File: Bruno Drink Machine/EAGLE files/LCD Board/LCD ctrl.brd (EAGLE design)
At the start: 82.5 x 76.2 mm, 36 parts, among them IC1 PIC24FJ256DA210-I/PT, IC2 IS62LV256AL, IC3 IS62LV256AL, IC4 BA3259H-HRP5, P1 CONN-40P-62684-401100ALF, P18 CONN-8P-PND, P2 USB-CON690-005-299-043

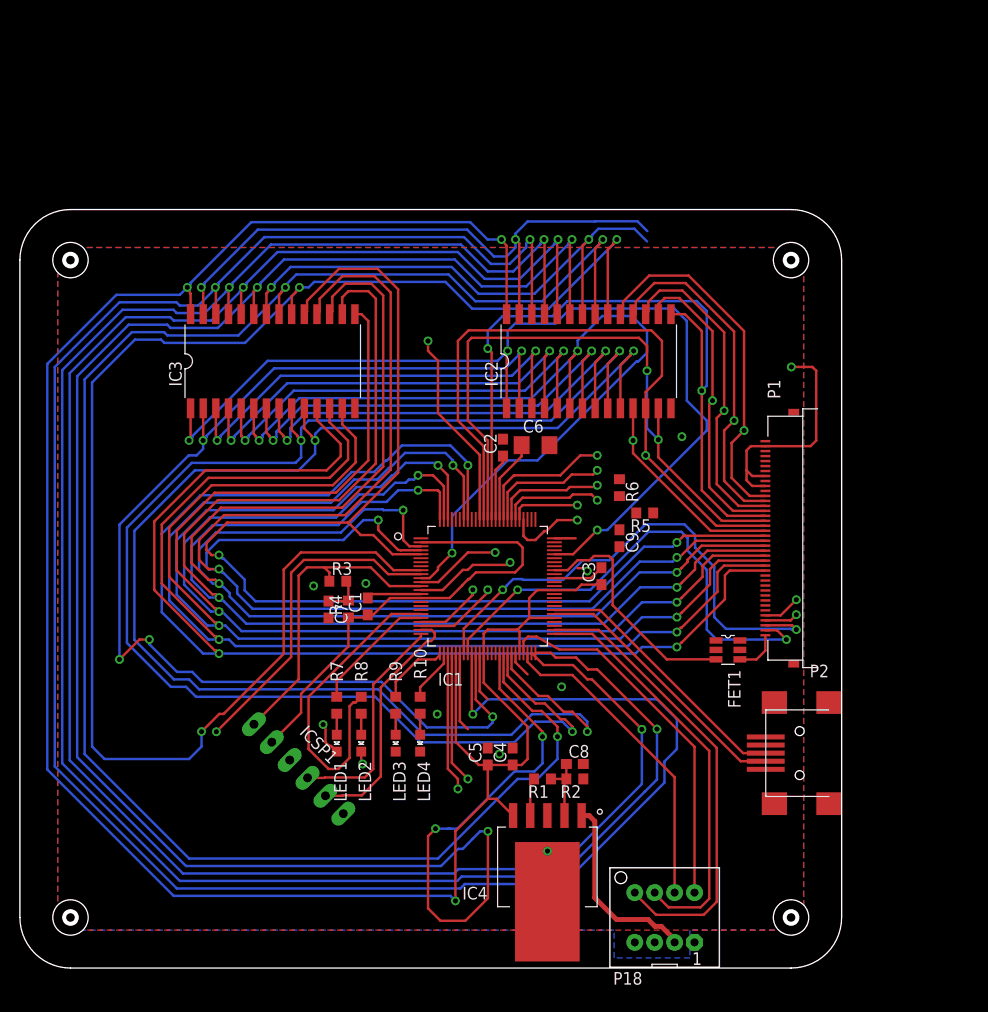
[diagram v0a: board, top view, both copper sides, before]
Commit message: airwires routed on LCD board; need to fix DRC errors before ordering PCBs
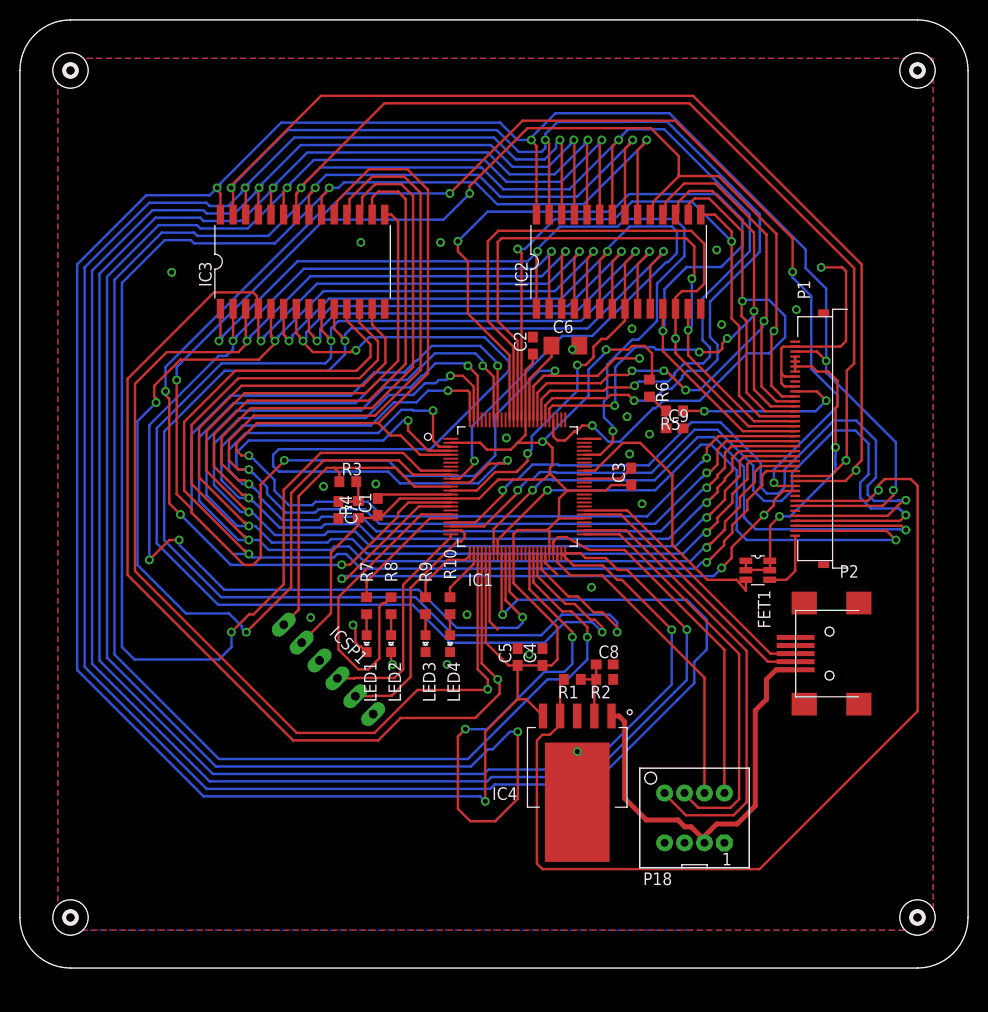
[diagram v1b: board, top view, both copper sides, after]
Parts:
- moved U$32 22.9 mm to (90.2, 90.2)
- moved U$33 19.0 mm to (5.08, 90.2)
- moved U$35 12.7 mm to (90.2, 5.08)
- moved C9 12.4 mm to (65.8, 54.2), turned to 0 degrees
- moved C2 10.7 mm to (51.5, 62.5)
- moved R5 10.7 mm to (65.8, 56.0)
- moved R6 10.4 mm to (63.2, 58.3)
- moved LED1 10.4 mm to (34.8, 32.6)
- moved LED2 10.4 mm to (37.3, 32.6)
- moved LED3 10.4 mm to (40.8, 32.6)
- moved LED4 10.4 mm to (43.2, 32.6)
- moved C3 10.4 mm to (61.4, 49.4)
- moved C4 10.4 mm to (52.5, 31.2)
- moved C5 10.4 mm to (50.0, 31.2)
- moved C6 10.4 mm to (54.8, 62.5)
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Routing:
- net DATA/!COMMAND: track 0.00 -> 157.0 mm, vias 0 -> 6
- net !WR: track 71.9 -> 212.9 mm, vias 3 -> 4
- net DB15: track 50.5 -> 185.6 mm, vias 2 -> 6
- net !RD: track 65.0 -> 192.6 mm, vias 3 -> 4
- net VCC: track 274.4 -> 378.7 mm, vias 3 -> 7
- net 1.8V: track 3.84 -> 101.6 mm, vias 0 -> 1
- net A6: track 58.5 -> 144.0 mm
- net A7: track 59.2 -> 135.2 mm
- net A3: track 54.5 -> 129.9 mm, vias 3 -> 4
- net XR: track 10.6 -> 78.2 mm
- net YU: track 11.7 -> 77.6 mm
- net !LCD_CS: track 0.00 -> 64.1 mm, vias 0 -> 3
- net DB8: track 41.1 -> 89.1 mm
- net A5: track 78.6 -> 126.0 mm, vias 3 -> 4
- net BL.C: track 0.00 -> 32.2 mm, vias 0 -> 2
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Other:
- board size 82.5 x 76.2 mm -> 95.2 x 95.2 mm

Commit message: fixed all DRC issues, Gerber files ready for ordering
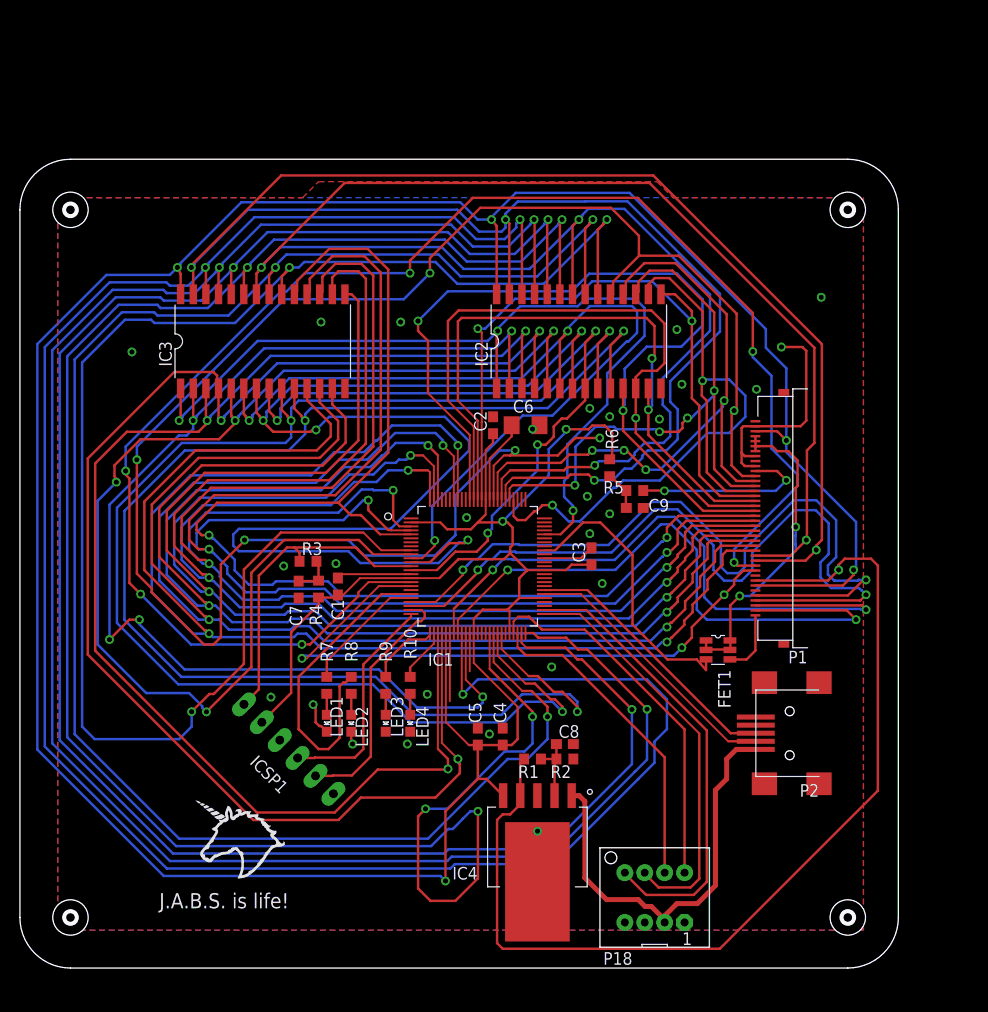
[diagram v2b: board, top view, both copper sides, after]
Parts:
- added U$20: (no value), Aaron:UNICORN-SCREEN
- added U$36: (no value), Aaron:JABS
- moved U$32 15.7 mm to (83.2, 76.2)
- moved U$33 14.0 mm to (5.08, 76.2)
- moved LED1 8.94 mm to (30.8, 24.6)
- moved LED2 8.94 mm to (33.3, 24.6)
- moved LED3 8.94 mm to (36.8, 24.6)
- moved LED4 8.94 mm to (39.2, 24.6)
- moved C1 8.94 mm to (31.9, 38.3)
- moved C2 8.94 mm to (47.5, 54.5)
- moved C3 8.94 mm to (57.4, 41.4)
- moved C4 8.94 mm to (48.5, 23.2)
- moved C5 8.94 mm to (46.0, 23.2)
- moved C6 8.94 mm to (50.8, 54.5)
- moved C7 8.94 mm to (28.0, 38.0)
- moved C8 8.94 mm to (54.8, 22.5)
- moved FET1 8.94 mm to (70.1, 32.0)
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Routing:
- net GND: track 64.7 -> 57.6 mm, vias 24 -> 27
- net D+: track 28.7 -> 27.2 mm
- net DATA/!COMMAND: track 157.0 -> 158.2 mm
- net DB5: track 148.0 -> 147.4 mm
- net A9: track 191.8 -> 192.4 mm
- net DB4: track 151.6 -> 151.0 mm
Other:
- board size 95.2 x 95.2 mm -> 88.2 x 81.2 mm

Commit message: fixed some minor silkscreen issues, moved USB connector to the edge of the PCB
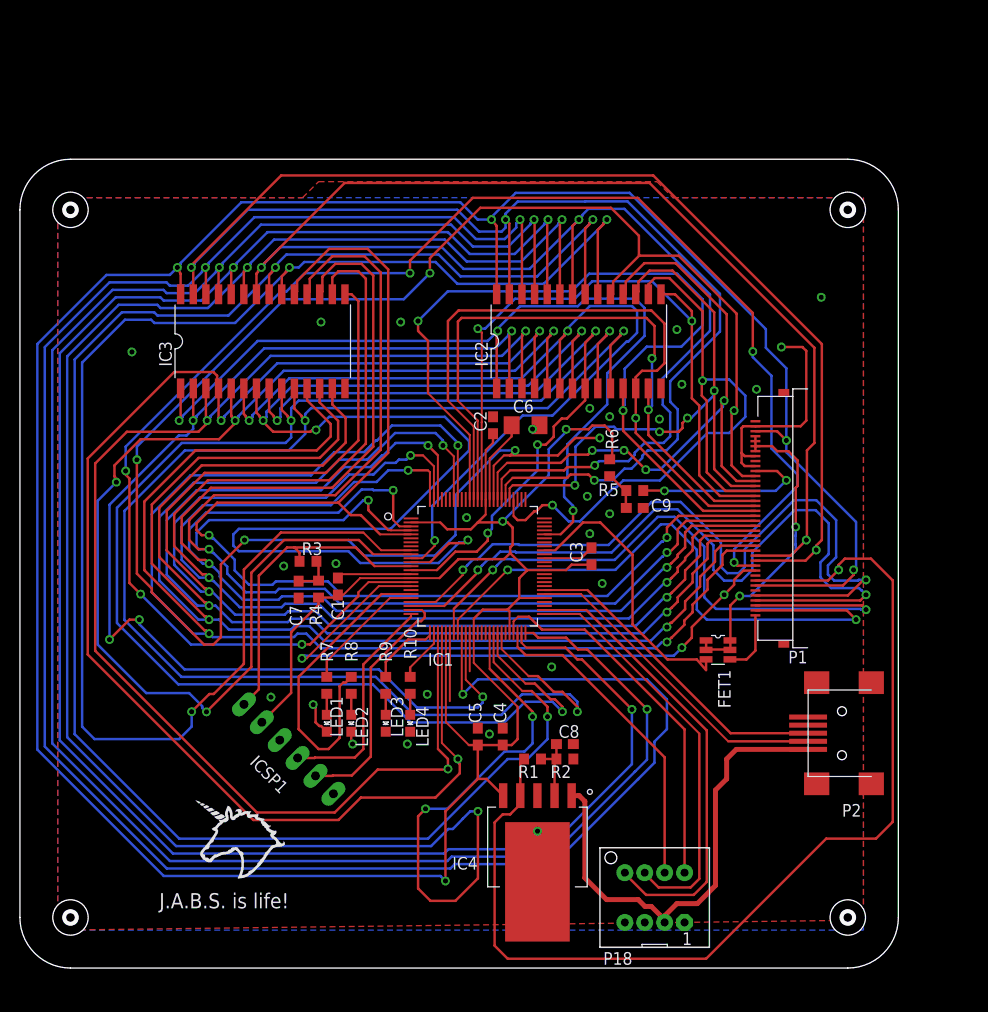
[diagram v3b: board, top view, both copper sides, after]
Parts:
- moved P2 5.25 mm to (85.5, 23.6)
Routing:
- net 1.8V: track 101.6 -> 106.9 mm
- net D-: track 27.4 -> 32.6 mm
- net +5V: track 42.8 -> 48.1 mm
- net D+: track 27.2 -> 32.4 mm
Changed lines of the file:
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@@
 <?xml version="1.0" encoding="utf-8"?>
 <!DOCTYPE eagle SYSTEM "eagle.dtd">
-<eagle version="9.2.2">
+<eagle version="8.2.2">
 <drawing>
 <settings>
 <setting alwaysvectorfont="yes"/>
-<setting keepoldvectorfont="yes"/>
 <setting verticaltext="up"/>
 </settings>
@@
 <layer number="45" name="Holes" color="7" fill="1" visible="yes" active="yes"/>
 <layer number="46" name="Milling" color="5" fill="1" visible="yes" active="yes"/>
-<layer number="47" name="Measures" color="7" fill="1" visible="no" active="yes"/>
+<layer number="47" name="Measures" color="7" fill="1" visible="yes" active="yes"/>
 <layer number="48" name="Document" color="7" fill="1" visible="no" active="yes"/>
 <layer number="49" name="Reference" color="7" fill="1" visible="no" active="yes"/>
@@
 <param name="dpMaxLengthDifference" value="10mm"/>
 <param name="dpGapFactor" value="2.5"/>
+<param name="checkGrid" value="0"/>
 <param name="checkAngle" value="0"/>
 <param name="checkFont" value="1"/>
 <param name="checkRestrict" value="1"/>
-<param name="checkStop" value="0"/>
-<param name="checkValues" value="0"/>
-<param name="checkNames" value="1"/>
-<param name="checkWireStubs" value="1"/>
-<param name="checkPolygonWidth" value="0"/>
 <param name="useDiameter" value="13"/>
 <param name="maxErrors" value="50"/>
@@
 </element>
 <element name="C3" library="rcl" package="C0603" value="0.1uF" x="57.42" y="41.37" smashed="yes" rot="R90">
-<attribute name="NAME" x="56.785" y="40.735" size="1.27" layer="25" rot="R90"/>
+<attribute name="NAME" x="56.535" y="40.735" size="1.27" layer="25" rot="R90"/>
 <attribute name="VALUE" x="59.325" y="40.735" size="1.27" layer="27" rot="R90"/>
 </element>
@@
 </element>
 <element name="C9" library="rcl" package="C0603" value="0.1uF" x="61.77" y="46.22" smashed="yes">
-<attribute name="NAME" x="63.135" y="45.855" size="1.27" layer="25"/>
+<attribute name="NAME" x="63.385" y="45.855" size="1.27" layer="25"/>
 <attribute name="VALUE" x="61.135" y="44.315" size="1.27" layer="27"/>
 </element>
@@
 </element>
 <element name="IC4" library="Aaron SMT" package="HRP5" value="BA3259H-HRP5" x="51.99" y="12.16" smashed="yes" rot="R180">
-<attribute name="NAME" x="45.99" y="10.16" size="1.27" layer="25" rot="R180"/>
+<attribute name="NAME" x="45.99" y="11.16" size="1.27" layer="25" rot="R180"/>
 <attribute name="VALUE" x="45.99" y="12.16" size="1.27" layer="27" rot="R180"/>
 </element>
@@
 <attribute name="NAME" x="58.595" y="0.33" size="1.27" layer="25"/>
 </element>
-<element name="P2" library="Aaron SMT" package="USB-CON(690-005-299-043)" value="USB-CON690-005-299-043" x="80.28" y="23.59" smashed="yes" rot="R90">
-<attribute name="NAME" x="80.28" y="18.48" size="1.27" layer="25" rot="R180"/>
+<element name="P2" library="Aaron SMT" package="USB-CON(690-005-299-043)" value="USB-CON690-005-299-043" x="85.53" y="23.59" smashed="yes" rot="R90">
+<attribute name="NAME" x="84.53" y="16.48" size="1.27" layer="25" rot="R180"/>
 </element>
 <element name="R1" library="rcl" package="R0603" value="1.5k" x="51.5" y="21" smashed="yes" rot="R180">
@@
 </element>
 <element name="R5" library="rcl" package="R0603" value="1.5k" x="61.77" y="47.97" smashed="yes" rot="R180">
-<attribute name="NAME" x="58.595" y="47.665" size="1.27" layer="25"/>
+<attribute name="NAME" x="58.095" y="47.415" size="1.27" layer="25"/>
 <attribute name="VALUE" x="62.405" y="49.875" size="1.27" layer="27" rot="R180"/>
 </element>
@@
 <vertex x="65.61" y="77.39"/>
 <vertex x="84.74" y="77.39"/>
-<vertex x="84.74" y="3.81"/>
+<vertex x="84.74" y="4.81"/>
 <vertex x="3.81" y="3.81"/>
 </polygon>
@@
 <wire x1="56.18" y1="17.32" x2="56.754" y2="16.746" width="0.5" layer="1"/>
 <contactref element="P2" pad="1"/>
-<wire x1="73.93" y1="21.9644" x2="71.9644" y2="21.9644" width="0.5" layer="1"/>
+<wire x1="79.18" y1="21.9644" x2="71.9644" y2="21.9644" width="0.5" layer="1"/>
 <wire x1="71.9644" y1="21.9644" x2="71" y2="21" width="0.5" layer="1"/>
 <wire x1="71" y1="21" x2="71" y2="19" width="0.5" layer="1"/>
@@
 <wire x1="49.25" y1="15.4375" x2="50.1875" y2="16.375" width="0.25" layer="1"/>
 <wire x1="48.5" y1="15.4375" x2="49.25" y2="15.4375" width="0.25" layer="1"/>
-<wire x1="47.9375" y1="14.875" x2="48.5" y2="15.4375" width="0.25" layer="1"/>
-<wire x1="47.9375" y1="2.5" x2="47.9375" y2="14.875" width="0.25" layer="1"/>
-<wire x1="48.5" y1="1.9375" x2="47.9375" y2="2.5" width="0.25" layer="1"/>
-<wire x1="70.3125" y1="1.9375" x2="48.5" y2="1.9375" width="0.25" layer="1"/>
-<wire x1="86.1875" y1="17.8125" x2="70.3125" y2="1.9375" width="0.25" layer="1"/>
-<wire x1="86.1875" y1="40.4375" x2="86.1875" y2="17.8125" width="0.25" layer="1"/>
-<wire x1="86.1875" y1="40.4375" x2="85.5" y2="41.125" width="0.25" layer="1"/>
+<wire x1="47.6875" y1="14.625" x2="48.5" y2="15.4375" width="0.25" layer="1"/>
+<wire x1="47.6875" y1="2.25" x2="47.6875" y2="14.625" width="0.25" layer="1"/>
+<wire x1="47.6875" y1="2.25" x2="49" y2="0.9375" width="0.25" layer="1"/>
+<wire x1="87.6875" y1="14.6875" x2="86" y2="13" width="0.25" layer="1"/>
+<wire x1="86" y1="13" x2="81" y2="13" width="0.25" layer="1"/>
+<wire x1="81" y1="13" x2="68.9375" y2="0.9375" width="0.25" layer="1"/>
+<wire x1="87.6875" y1="38.9375" x2="87.6875" y2="14.6875" width="0.25" layer="1"/>
+<wire x1="87.6875" y1="38.9375" x2="85.5" y2="41.125" width="0.25" layer="1"/>
 <wire x1="50.1875" y1="17.3125" x2="50.27" y2="17.32" width="0.25" layer="1"/>
 <wire x1="82.875" y1="41.125" x2="85.5" y2="41.125" width="0.25" layer="1"/>
 <wire x1="82.25" y1="40" x2="82.25" y2="40.5" width="0.25" layer="1"/>
 <wire x1="82.25" y1="40.5" x2="82.875" y2="41.125" width="0.25" layer="1"/>
+<wire x1="49" y1="0.9375" x2="68.9375" y2="0.9375" width="0.25" layer="1"/>
 </signal>
 <signal name="BL.C">
@@
 <contactref element="P2" pad="3"/>
 <contactref element="IC1" pad="57"/>
-<wire x1="71.40265" y1="23.59" x2="73.93" y2="23.59" width="0.25" layer="1"/>
+<wire x1="71.40265" y1="23.59" x2="79.18" y2="23.59" width="0.25" layer="1"/>
 <wire x1="52.69" y1="37.97" x2="57.02265" y2="37.97" width="0.2" layer="1"/>
 <wire x1="57.02265" y1="37.97" x2="71.40265" y2="23.59" width="0.25" layer="1"/>
@@
 <contactref element="P2" pad="2"/>
 <contactref element="IC1" pad="56"/>
-<wire x1="71.1547875" y1="22.7772" x2="73.93" y2="22.7772" width="0.25" layer="1"/>
+<wire x1="71.1547875" y1="22.7772" x2="79.18" y2="22.7772" width="0.25" layer="1"/>
 <wire x1="52.69" y1="37.57" x2="56.3619875" y2="37.57" width="0.2" layer="1"/>
 <wire x1="56.3619875" y1="37.57" x2="71.1547875" y2="22.7772" width="0.2" layer="1"/>
@@
 </signal>
 </signals>
-<mfgpreviewcolors>
-<mfgpreviewcolor name="soldermaskcolor" color="0xC8008000"/>
-<mfgpreviewcolor name="silkscreencolor" color="0xFFFEFEFE"/>
-<mfgpreviewcolor name="backgroundcolor" color="0xFF282828"/>
-<mfgpreviewcolor name="coppercolor" color="0xFFFFBF00"/>
-<mfgpreviewcolor name="substratecolor" color="0xFF786E46"/>
-</mfgpreviewcolors>
 <errors>
 </errors>

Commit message: commit before merge
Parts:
- renumbered P18 to P3
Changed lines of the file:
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@@
 <attribute name="VALUE" x="77.39" y="59.18" size="1.27" layer="27" rot="R90"/>
 </element>
-<element name="P18" library="Aaron" package="B08B-PND" value="CONN-8P-PND" x="63.77" y="7.08" smashed="yes">
+<element name="P3" library="Aaron" package="B08B-PND" value="CONN-8P-PND" x="63.77" y="7.08" smashed="yes">
 <attribute name="NAME" x="58.595" y="0.33" size="1.27" layer="25"/>
 </element>
@@
 <signals>
 <signal name="GND">
-<contactref element="P18" pad="3"/>
+<contactref element="P3" pad="3"/>
 <contactref element="P1" pad="40"/>
 <contactref element="P1" pad="8"/>
@@
 <vertex x="65.61" y="77.39"/>
 <vertex x="84.74" y="77.39"/>
-<vertex x="84.74" y="4.81"/>
+<vertex x="84.74" y="3.81"/>
 <vertex x="3.81" y="3.81"/>
 </polygon>
@@
 </signal>
 <signal name="12V">
-<contactref element="P18" pad="1"/>
+<contactref element="P3" pad="1"/>
 </signal>
 <signal name="MOSI">
-<contactref element="P18" pad="5"/>
+<contactref element="P3" pad="5"/>
 <contactref element="IC1" pad="52"/>
 <wire x1="67.69463125" y1="7.34775" x2="69.00225" y2="8.65536875" width="0.25" layer="1"/>
@@
 </signal>
 <signal name="SCK">
-<contactref element="P18" pad="7"/>
+<contactref element="P3" pad="7"/>
 <contactref element="IC1" pad="48"/>
 <wire x1="64.77" y1="9.58" x2="64.77" y2="21.1693375" width="0.25" layer="1"/>
@@
 </signal>
 <signal name="!SS">
-<contactref element="P18" pad="8"/>
+<contactref element="P3" pad="8"/>
 <contactref element="IC1" pad="47"/>
 <wire x1="66.77" y1="9.58" x2="66.77" y2="23.98" width="0.25" layer="1"/>
@@
 </signal>
 <signal name="MISO">
-<contactref element="P18" pad="6"/>
+<contactref element="P3" pad="6"/>
 <contactref element="IC1" pad="51"/>
 <wire x1="63.28775" y1="8.96603125" x2="64.15603125" y2="8.09775" width="0.25" layer="1"/>
@@
 </signal>
 <signal name="+5V" class="1">
-<contactref element="P18" pad="2"/>
+<contactref element="P3" pad="2"/>
 <contactref element="IC4" pad="1"/>
 <wire x1="64.37725" y1="5.24575" x2="63.43575" y2="6.18725" width="0.5" layer="1"/>
